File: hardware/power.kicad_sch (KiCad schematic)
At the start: 36 parts, among them U101 ECP5U_85_CABGA756, U201 TPS62290, U202 TPS62290, U203 TPS62290, U204 TPS62290, U206 TPS62290

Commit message: Save
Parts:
- C201: renamed from C101; Comment (none) -> X5R,25V
- C202: renamed from C102; Comment (none) -> X5R,25V
- C203: renamed from C103; Comment (none) -> X5R,25V
- C204, C215: renamed from C104; Comment (none) -> X5R,25V
- R201: renamed from R101; footprint passive:R_0402 -> passive:R_0201
- R202: renamed from R102; footprint passive:R_0402 -> passive:R_0201
- R203: renamed from R103; footprint passive:R_0402 -> passive:R_0201
- R204: renamed from R104; footprint passive:R_0402 -> passive:R_0201
- R205: renamed from R105; footprint passive:R_0402 -> passive:R_0201
- R206: renamed from R106; footprint passive:R_0402 -> passive:R_0201
- R207, R209: renamed from R107; footprint passive:R_0402 -> passive:R_0201
- R208, R210: renamed from R108; footprint passive:R_0402 -> passive:R_0201
- renumbered C105 to C205, C106 to C206, C107 to C207, C108 to C208, C109 to C209, C110 to C210, C111 to C211, C112 to C212, C108 to C216, C112 to C217, L101 to L201, L101 to L202, L101 to L203, L101 to L204, L101 to L205

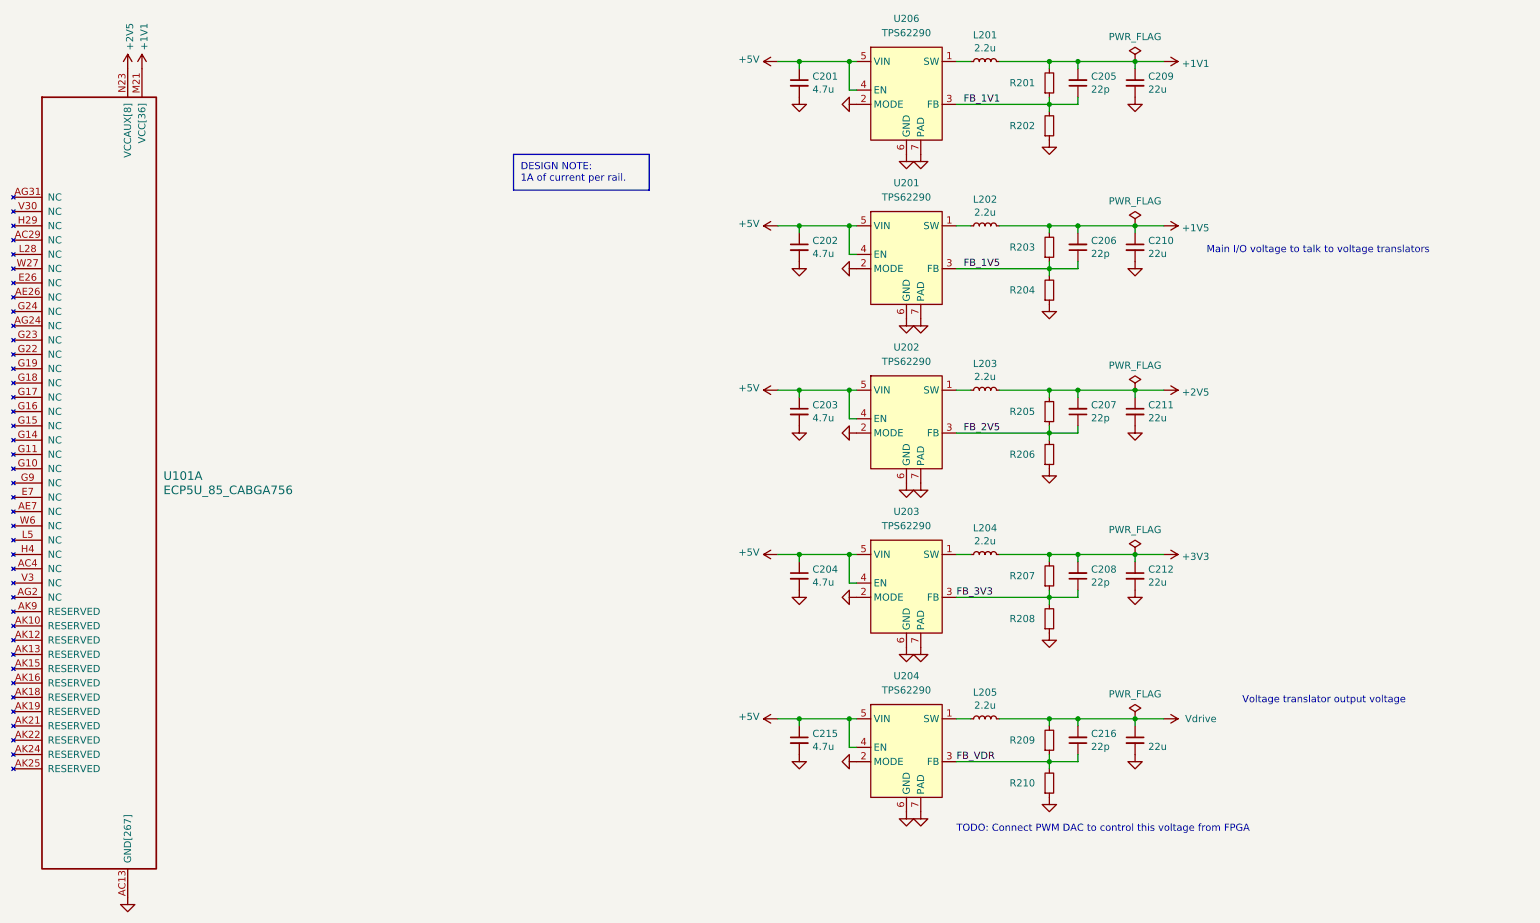
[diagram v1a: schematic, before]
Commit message: Moved to PCIe connectors, added USB 3.0 Type B connector
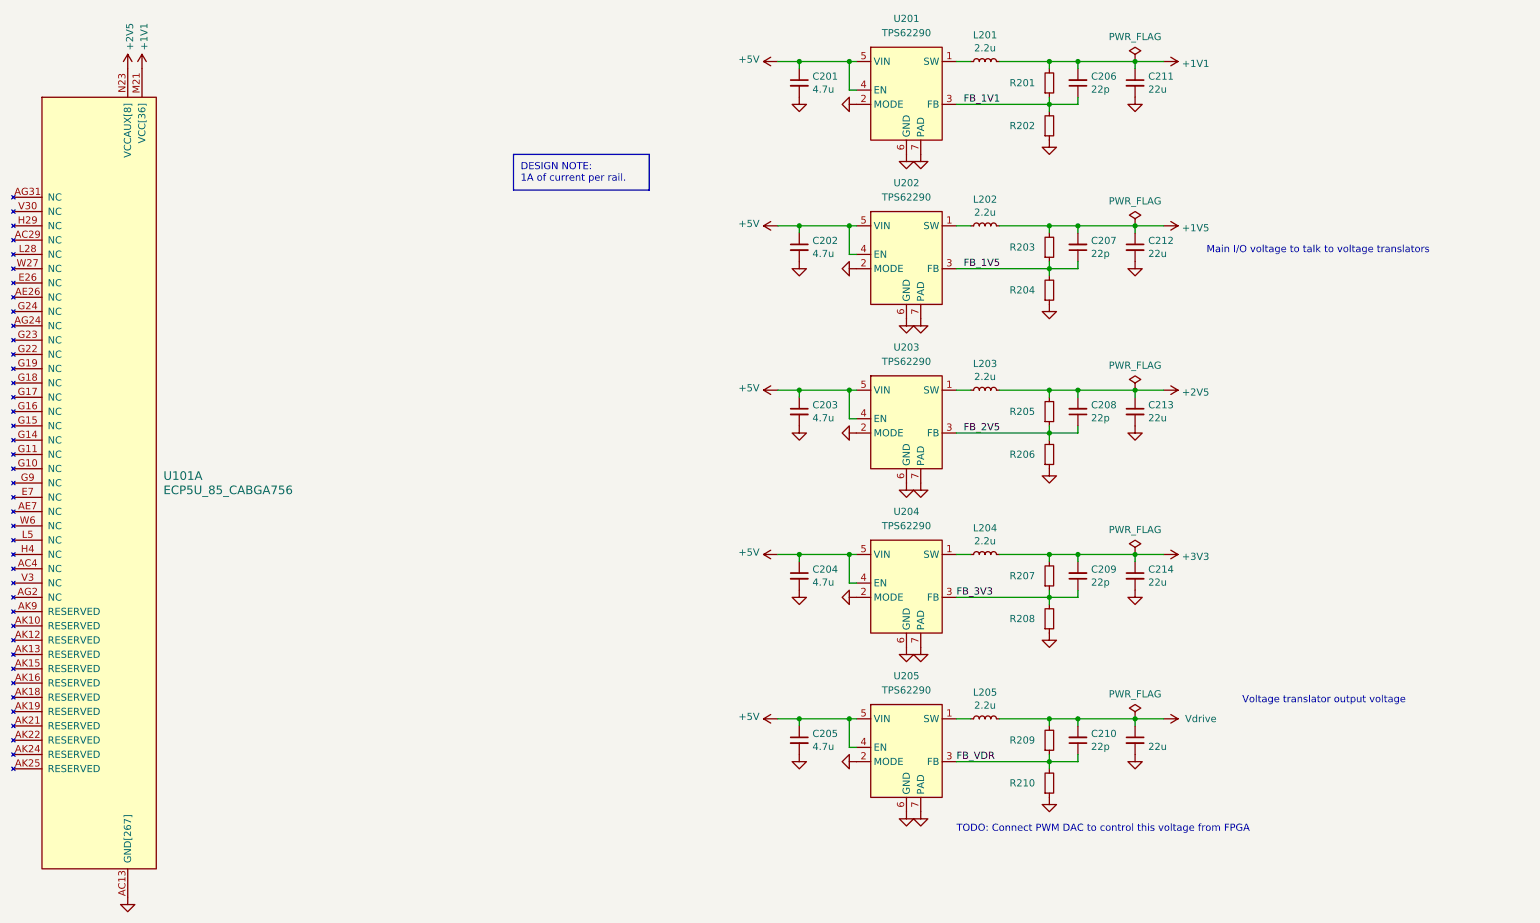
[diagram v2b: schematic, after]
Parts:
- renumbered C215 to C205, C205 to C206, C206 to C207, C207 to C208, C208 to C209, C216 to C210, C209 to C211, C210 to C212, C211 to C213, C212 to C214, C217 to C215, U206 to U201, U201 to U202, U202 to U203, U203 to U204, U204 to U205

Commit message: Save
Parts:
- removed C205: 4.7u, passive:C_0603, symbol Device:C_Small
- removed C210: 22p, passive:C_0402, symbol Device:C_Small
- removed C215: 22u, passive:C_0603, symbol Device:C_Small
- removed L205: 2.2u, Inductor_SMD:L_Abracon_ASPI-3012S, symbol Device:L_Small
- removed R209, R210: ~, passive:R_0201, symbol Device:R_Small
- removed U205: TPS62290, Package_SON:WSON-6-1EP_2x2mm_P0.65mm_EP1x1.6mm, symbol dc_dc_regulators:TPS62290
- C206, C207, C208, C209: footprint passive:C_0402 -> passive:C_0201
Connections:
- net +1V5 is gone; now on net Vdrive: C207.2, C212.1, L202.2, R203.2
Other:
- note removed: "Voltage translator output voltage"
- moved on the sheet: C202, C203, C204, C207, C208, C209, C212, C213, C214, L202, L203, L204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

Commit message: Save
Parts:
- added C205: 4.7u, passive:C_0603, symbol Device:C_Small
- added C210: 22p, passive:C_0201, symbol Device:C_Small
- added C215: 22u, passive:C_0603, symbol Device:C_Small
- added L205: 2.2u, Inductor_SMD:L_Abracon_ASPI-3012S, symbol Device:L_Small
- added R209, R210: ~, passive:R_0201, symbol Device:R_Small
- added U205: TPS62290, Package_SON:WSON-6-1EP_2x2mm_P0.65mm_EP1x1.6mm, symbol dc_dc_regulators:TPS62290
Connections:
- net +5V: now also C205.1, U205.4 (EN), U205.5 (VIN)
- net FB_3V3: now also C210.1, R209.1, R210.2, U205.3 (FB)
- net GND: now also C205.2, C215.2, R210.1, U205.2 (MODE), U205.6 (GND), U205.7 (PAD)
- new net: L205.1, U205.1 (SW)
- new net +1V5: C210.2, C215.1, L205.2, R209.2

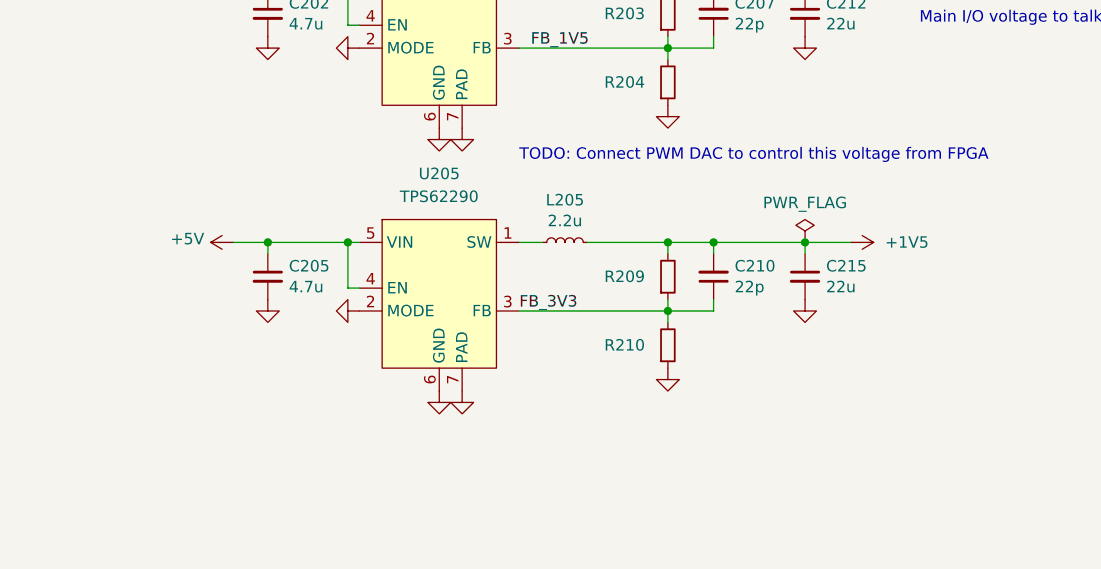
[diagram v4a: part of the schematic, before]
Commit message: Moved to new level translator with less input current requirement
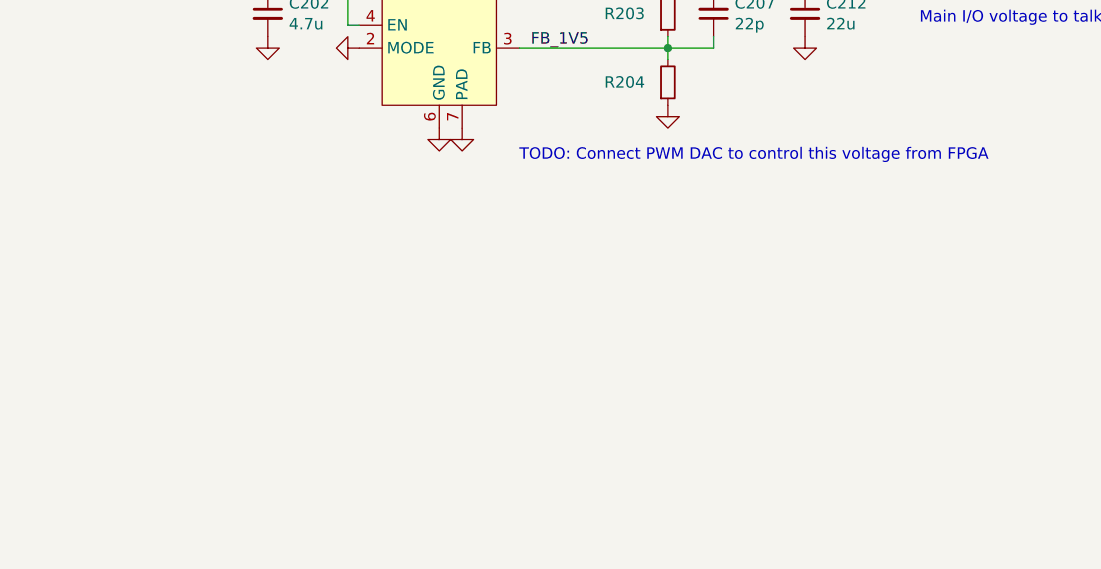
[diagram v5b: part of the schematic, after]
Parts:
- removed C205: 4.7u, passive:C_0603, symbol Device:C_Small
- removed C210: 22p, passive:C_0201, symbol Device:C_Small
- removed C215: 22u, passive:C_0603, symbol Device:C_Small
- removed L205: 2.2u, Inductor_SMD:L_Abracon_ASPI-3012S, symbol Device:L_Small
- removed R209, R210: ~, passive:R_0201, symbol Device:R_Small
- removed U205: TPS62290, Package_SON:WSON-6-1EP_2x2mm_P0.65mm_EP1x1.6mm, symbol dc_dc_regulators:TPS62290
- C206, C207, C208, C209: footprint passive:C_0201 -> passive:C_0402
- R201, R202, R203, R204, R205, R206, R207, R208: footprint passive:R_0201 -> passive:R_0402
